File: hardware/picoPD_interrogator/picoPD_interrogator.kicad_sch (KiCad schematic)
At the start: 55 parts, among them J1 Conn_01x07, J2 USB_C_Receptacle_USB2.0_16P, J3 Conn_01x14, Q1 rohm-RE1C002UN, Q2 rohm-RE1C002UN, Q3 rohm-RE1C002UN, Q4 rohm-RE1C002UN, Q5 rohm-RE1C002UN, SW1 RESET_BTN, U2 FUSB302BMPX, U3 ST-LM393QT, U6 LV2862XDDC

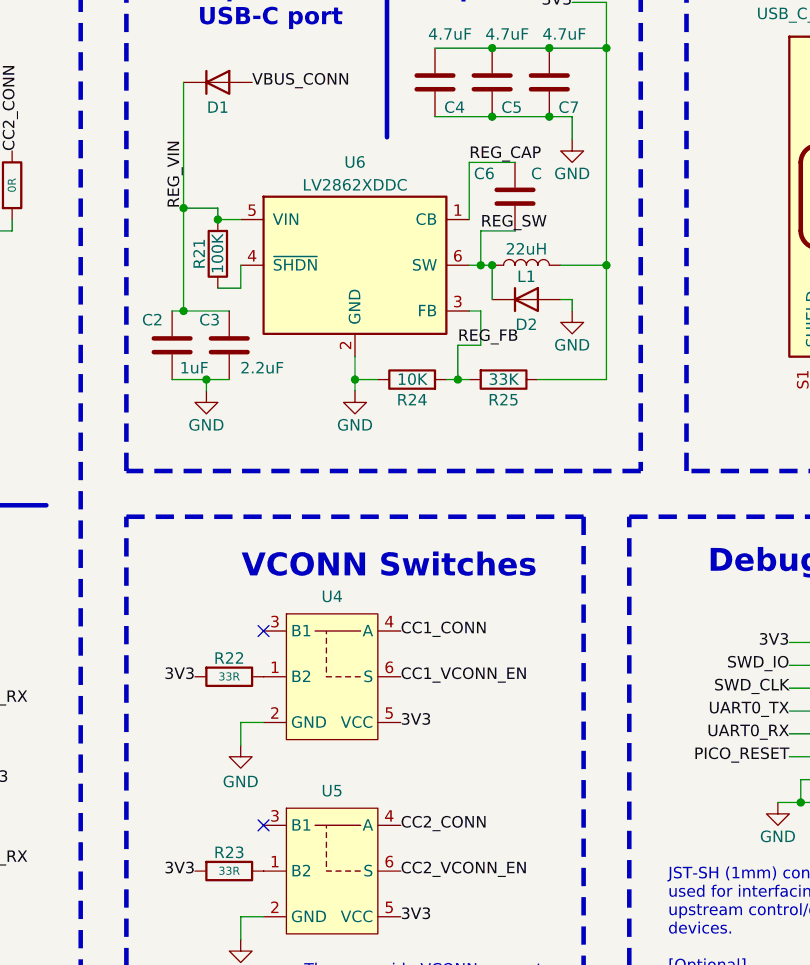
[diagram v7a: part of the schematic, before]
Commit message: BOM: Adjusted values for a few diodes and capacitors.
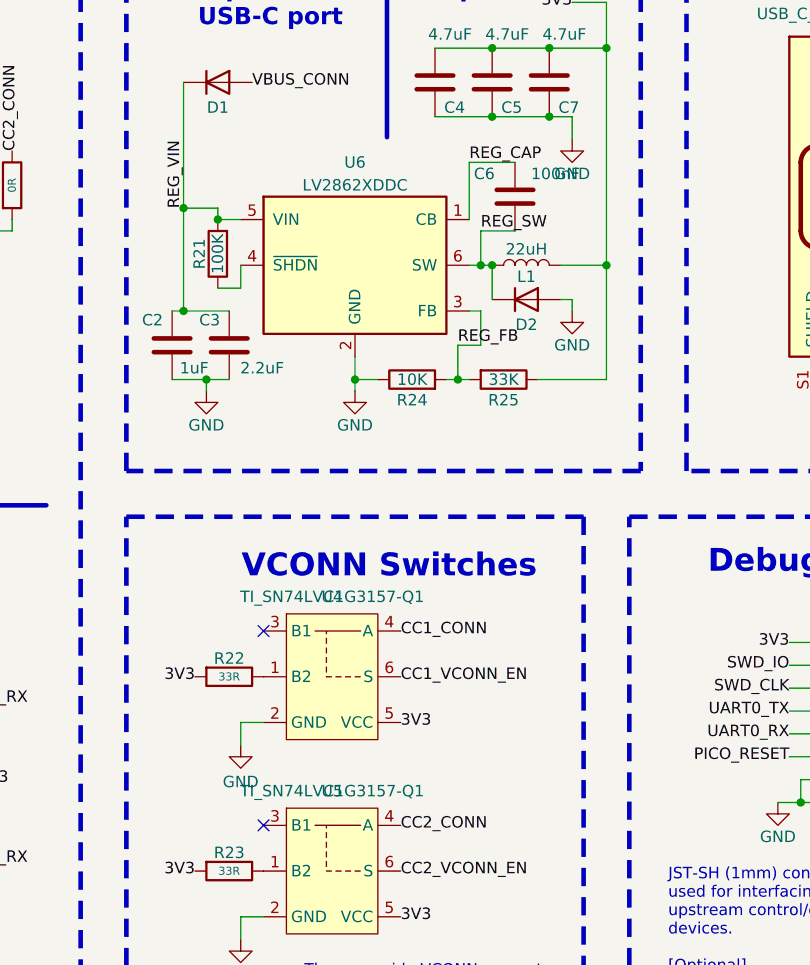
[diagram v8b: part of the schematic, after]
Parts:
- C6: value C -> 100nF
- D1, D2: value D -> DSS16U
- U4, U5: value ~ -> TI_SN74LVC1G3157-Q1
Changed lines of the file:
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@@
 			)
 		)
-		(property "Value" "C"
+		(property "Value" "100nF"
 			(at 208.788 49.53 0)
 			(effects
@@
 			)
 		)
-		(property "Value" "D"
+		(property "Value" "DSS16U"
 			(at 172.466 42.418 0)
 			(effects
@@
 			)
 		)
-		(property "Value" "~"
+		(property "Value" "TI_SN74LVC1G3157-Q1"
 			(at 186.69 96.52 0)
 			(effects
@@
 			)
 		)
-		(property "Value" "D"
+		(property "Value" "DSS16U"
 			(at 206.756 66.548 0)
 			(effects
@@
 			)
 		)
-		(property "Value" "~"
+		(property "Value" "TI_SN74LVC1G3157-Q1"
 			(at 186.69 118.11 0)
 			(effects
